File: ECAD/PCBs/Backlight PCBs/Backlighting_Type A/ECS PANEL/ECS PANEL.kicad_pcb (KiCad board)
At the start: 2 copper layers, 133.6 x 93 mm, 146 parts, among them J1 Conn_01x04_Female, J2 Conn_01x04_Female

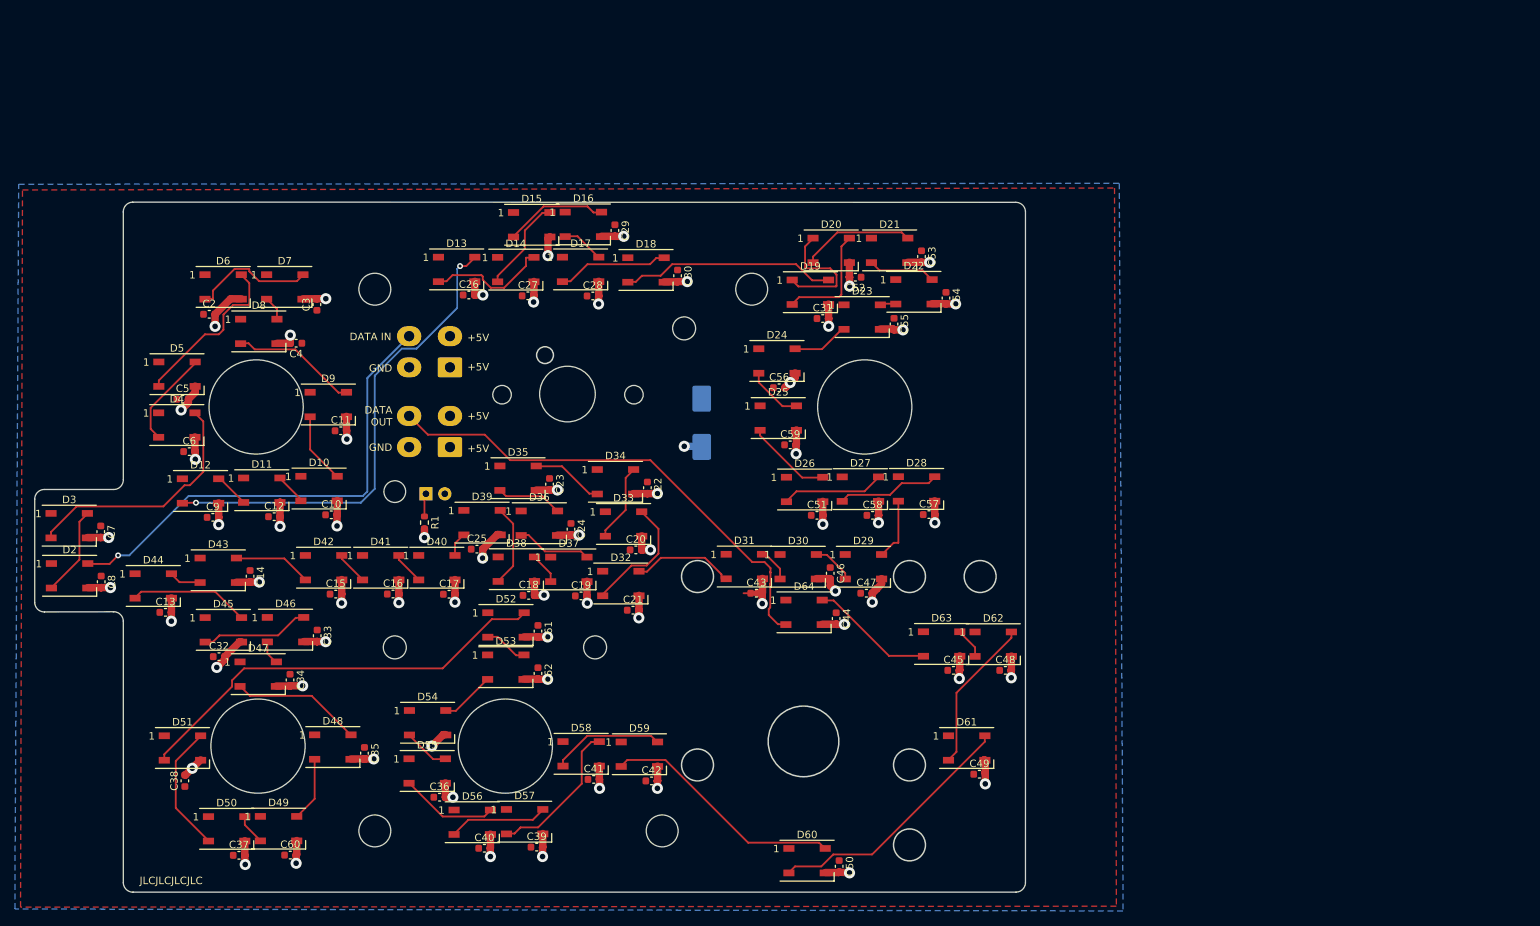
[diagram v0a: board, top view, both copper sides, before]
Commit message: Drawing Sheet & Silkscreen update - Backlight Panels(An - Fc)
1:  Updated/Relinked Drawing Sheet for both PCB and Schematics
2:  Standardized Silkscreen (if required)
3:  Added WS2812B symbol to OH Library (for future schematic fixing)

ANT SEL thru FCS PANEL
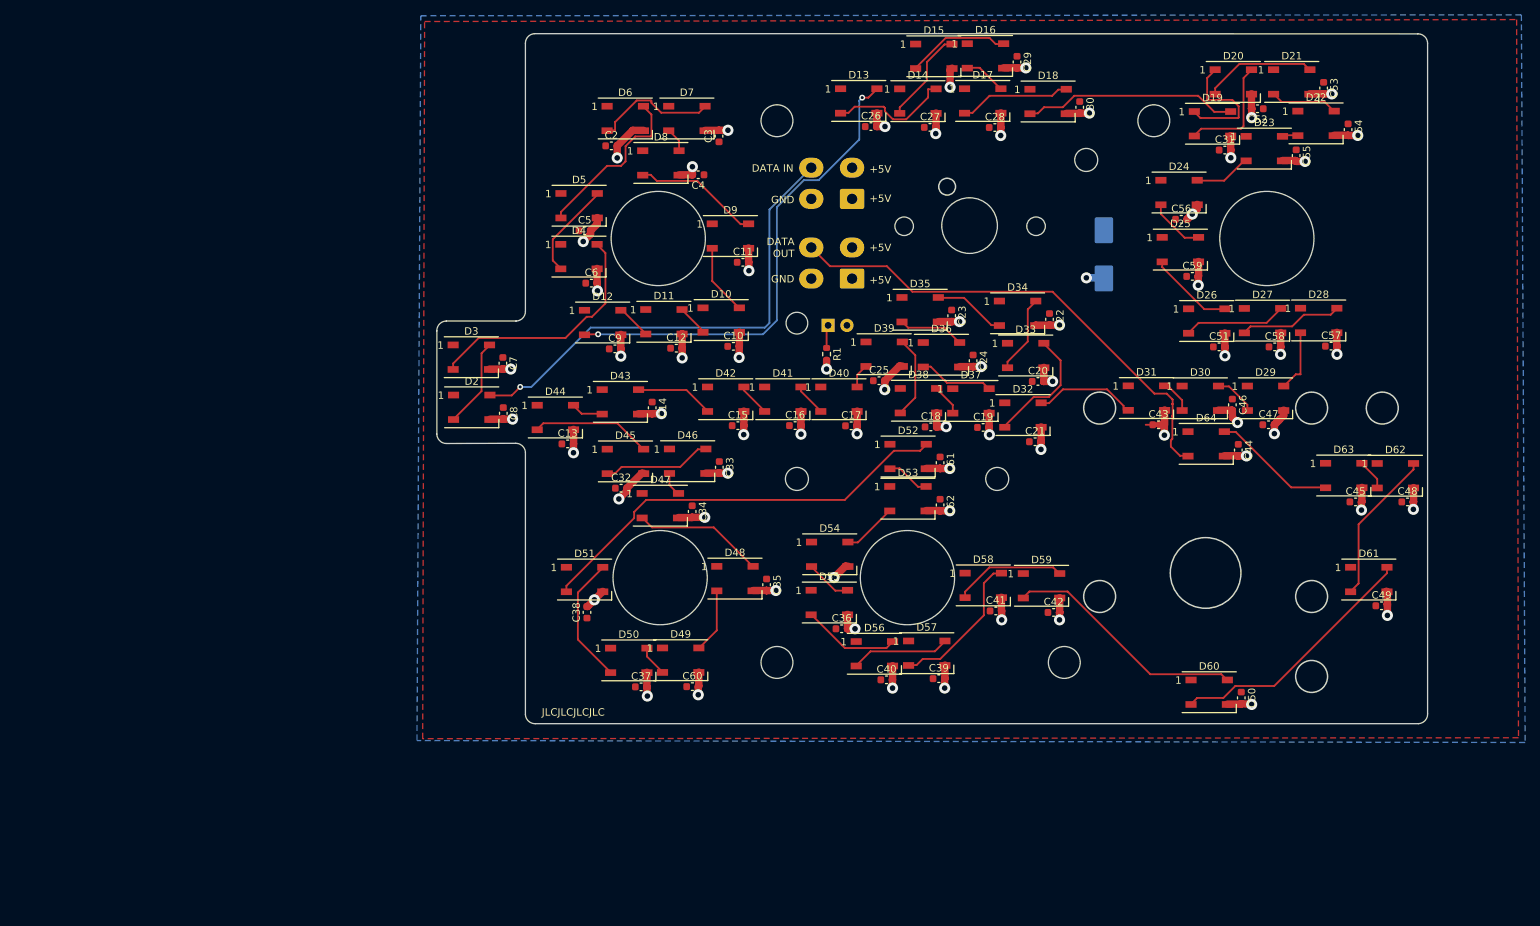
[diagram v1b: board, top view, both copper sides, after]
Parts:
- moved G*** 63.7 mm to (104.0, 93.6)
- moved C17 58.8 mm to (131.5, 97.1)
- moved C25 58.8 mm to (135.3, 91.1)
- moved C26 58.8 mm to (134.2, 56.8)
- moved C31 58.8 mm to (181.9, 60.0)
- moved C40 58.8 mm to (136.3, 131.4)
- moved C43 58.8 mm to (173.0, 97.0)
- moved C46 58.8 mm to (182.9, 94.3)
- moved C5 58.8 mm to (95.6, 70.8)
- moved C59 58.8 mm to (177.5, 77.0)
- moved D12 58.8 mm to (98.0, 83.2)
- moved D13 58.8 mm to (132.5, 53.3)
- moved D15 58.8 mm to (142.7, 47.3)
- moved D17 58.8 mm to (149.3, 53.3)
- moved D18 58.8 mm to (158.1, 53.4)
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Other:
- board text added: "ECS PANEL Revision: 3 www.openhornet.com"
- board text removed: "ECS Panel Backlight Designed by L. Walker"
- board text removed: "Version 2.0"

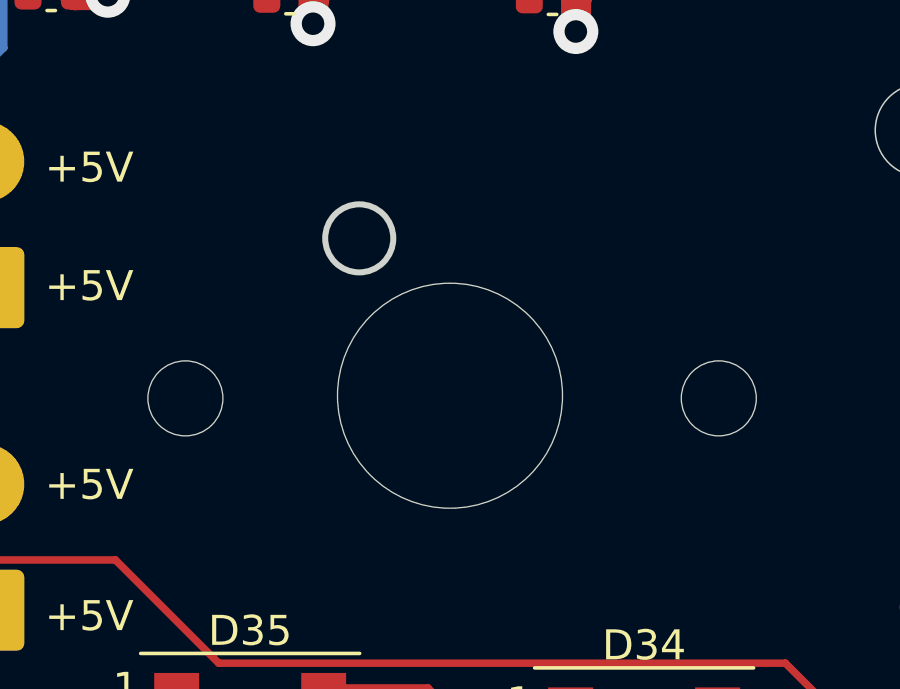
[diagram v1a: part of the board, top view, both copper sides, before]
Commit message: Review: ECS thru FCS  100%
Reviewed/adjusted silkscreens as needed
Relinked footprints
Updated Manufacturing files
Updated PNGs and STEP files as needed.
Renamed a few PNGs for standardization
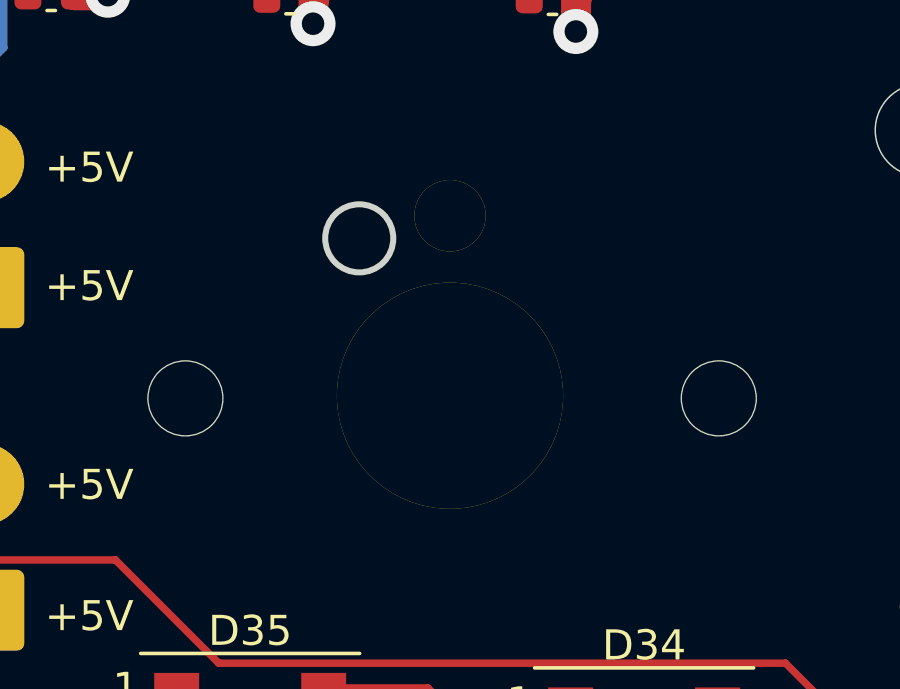
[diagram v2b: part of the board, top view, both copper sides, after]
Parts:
- 1, 3: footprint OH_Backlighting:SxAL_Toggle_13x13mm -> OH_Footprints:SxAL_Toggle_13x13mm
- 5, REF**: footprint OH_Backlighting:631H_Toggle_13mm_x_13mm -> OH_Footprints:631H_Toggle_13mm_x_13mm
- G*** (x2): footprint OH_Backlighting:S3AL_Toggle_Silkscreen -> OH_Footprints:S3AL_Toggle_Silkscreen
- G*** (x2): footprint OH_Backlighting:631H_Toggle_Silkscreen -> OH_Footprints:631H_Toggle_Silkscreen
- G***: footprint OH_General:CC-BY-NC-SA-Small -> OH_Footprints:CC-BY-NC-SA-Small
- G***: footprint OH_General:OH_LOGO_37.7mm_5.9mm -> OH_Footprints:OH_LOGO_37.7mm_5.9mm
- REF**: footprint OH_Backlighting:BR10K_Pot_11mm_x_11mm -> OH_Footprints:BR10K_Pot_11mm_x_11mm
- REF** (x4): footprint OH_Backlighting:OH_Panel_6-32_PHS -> OH_Footprints:OH_Panel_6-32_PHS
- REF** (x2): value MountingHole_2.5mm -> MountingHole; footprint MountingHole:MountingHole_2.5mm -> OH_Footprints:MountingHole_2.5mm

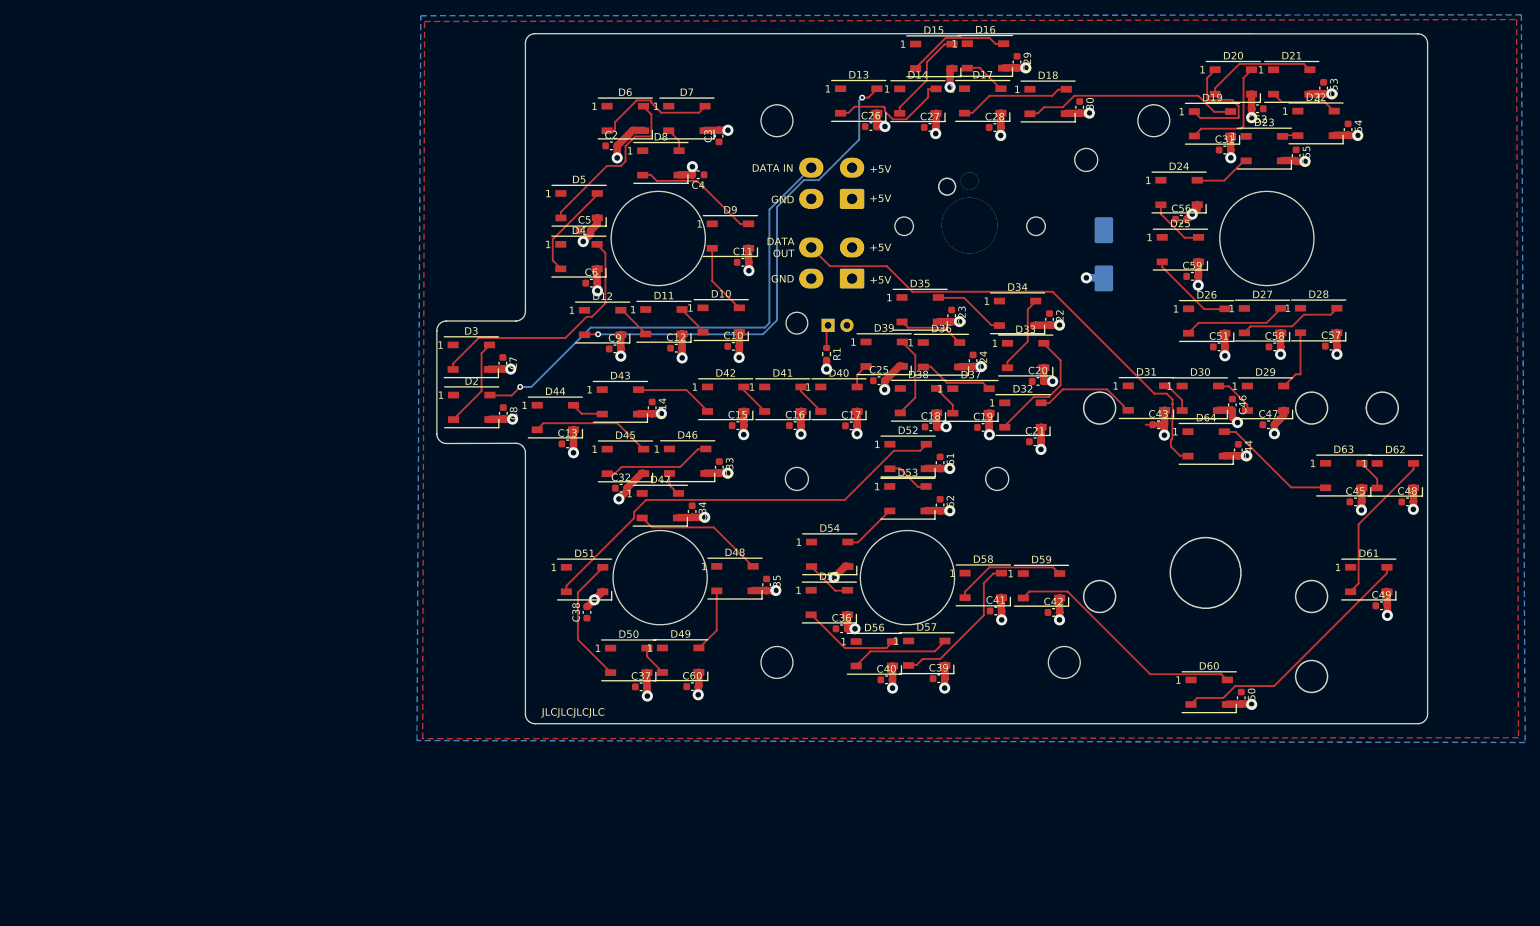
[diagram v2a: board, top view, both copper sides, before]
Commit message: KiCad 7 Transition - ECS Panel
Changed orientation of Test Point symbol in library from +90 to 0

Schematic/PCB standardization
-Consolidated BOM.  Removed excess BOMs
-Updated manufacturing files
-Fixed PCB routing after rotating a LED 90 degress.  Pad didn't have access to GND net.
-Fixed clearance issues around NPTHs
-Updated Assets (PNGs, STEP)
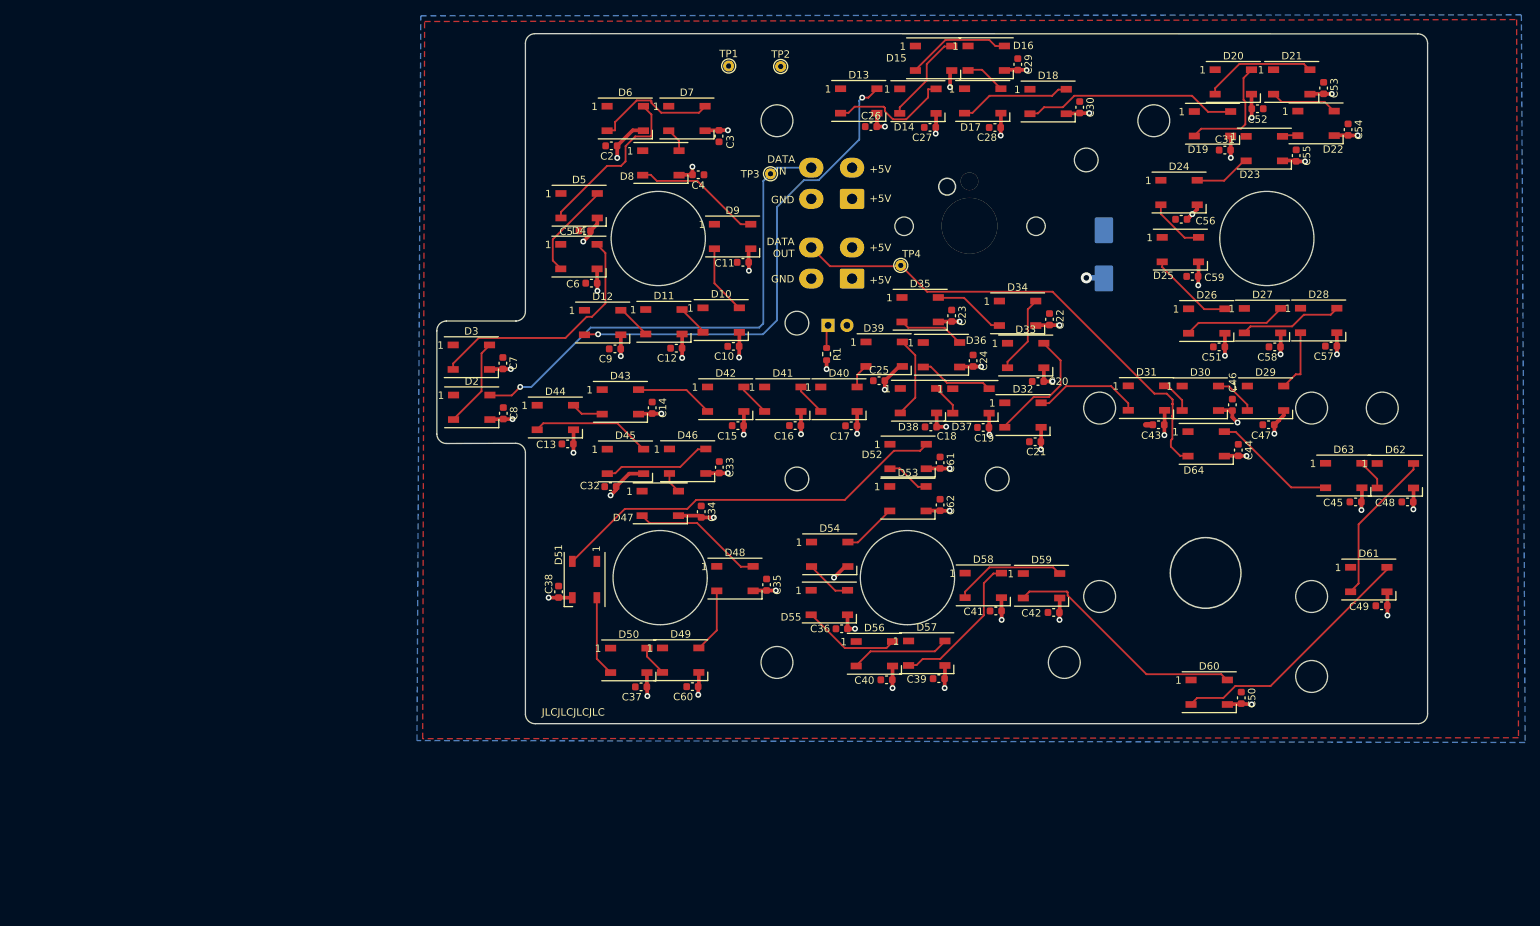
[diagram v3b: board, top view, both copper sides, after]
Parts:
- removed 1, 3: SxAL_Toggle_13x13mm, OH_Footprints:SxAL_Toggle_13x13mm
- removed 5, REF**: 631H_Toggle_13mm_x_13mm, OH_Footprints:631H_Toggle_13mm_x_13mm
- removed REF**: BR10K_Pot_11mm_x_11mm, OH_Footprints:BR10K_Pot_11mm_x_11mm
- removed REF** (x4): OH_Panel_Fastner_Keepout, OH_Footprints:OH_Panel_6-32_PHS
- removed REF** (x2): MountingHole, OH_Footprints:MountingHole_2.5mm
- added MH1: 6x32 / 4mm, OH_Footprints:MountingHole_6-32_PHS, B.Cu at (121.5, 56.0)
- added MH10: 6x32 / 4mm, OH_Footprints:MountingHole_6-32_PHS, B.Cu at (193.6, 130.9)
- added MH11: M3 / 3.2mm, OH_Footprints:MountingHole_3.2mm_M3_DIN965, B.Cu at (163.2, 61.3)
- added MH12: M3 / 3.2mm, OH_Footprints:MountingHole_3.2mm_M3_DIN965, B.Cu at (124.2, 83.3)
- added MH13: M3 / 3.2mm, OH_Footprints:MountingHole_3.2mm_M3_DIN965, B.Cu at (124.2, 104.3)
- added MH14: M3 / 3.2mm, OH_Footprints:MountingHole_3.2mm_M3_DIN965, B.Cu at (151.2, 104.3)
- added MH15: 2.5mm, OH_Footprints:MountingHole_2.5mm, B.Cu at (138.7, 70.2)
- added MH16: 2.5mm, OH_Footprints:MountingHole_2.5mm, B.Cu at (156.4, 70.2)
- added MH17: Switch_NKK SxAL, OH_Footprints:SxAL_Toggle_13x13mm, F.Cu at (105.5, 71.9)
- added MH18: Switch_NKK SxAL, OH_Footprints:SxAL_Toggle_13x13mm, F.Cu at (187.6, 71.9)
- added MH19: Switch_631H, OH_Footprints:631HX_Toggle_13mm_x_13mm, F.Cu at (105.8, 117.6)
- added MH2: 6x32 / 4mm, OH_Footprints:MountingHole_6-32_PHS, B.Cu at (172.3, 56.0)
- added MH20: Switch_631H, OH_Footprints:631HX_Toggle_13mm_x_13mm, F.Cu at (139.1, 117.6)
- added MH21: Pot_B10K, OH_Footprints:BR10K_Pot_11mm_x_11mm, F.Cu at (147.5, 70.2)
- added MH3: 6x32 / 4mm, OH_Footprints:MountingHole_6-32_PHS, B.Cu at (165.0, 94.7)
- added MH4: 6x32 / 4mm, OH_Footprints:MountingHole_6-32_PHS, B.Cu at (193.6, 94.7)
- added MH5: 6x32 / 4mm, OH_Footprints:MountingHole_6-32_PHS, B.Cu at (203.1, 94.7)
- added MH6: 6x32 / 4mm, OH_Footprints:MountingHole_6-32_PHS, B.Cu at (165.0, 120.1)
- added MH7: 6x32 / 4mm, OH_Footprints:MountingHole_6-32_PHS, B.Cu at (193.6, 120.1)
- added MH8: 6x32 / 4mm, OH_Footprints:MountingHole_6-32_PHS, B.Cu at (121.5, 129.0)
- added MH9: 6x32 / 4mm, OH_Footprints:MountingHole_6-32_PHS, B.Cu at (160.3, 129.0)
- added TP1: TestPoint, OH_Footprints:TestPoint_THTPad_D1.5mm_Drill0.7mm, F.Cu at (115.0, 48.6)
- added TP2: TestPoint, OH_Footprints:TestPoint_THTPad_D1.5mm_Drill0.7mm, F.Cu at (122.0, 48.7)
- added TP3: TestPoint, OH_Footprints:TestPoint_THTPad_D1.5mm_Drill0.7mm, F.Cu at (120.6, 63.2)
- added TP4: TestPoint, OH_Footprints:TestPoint_THTPad_D1.5mm_Drill0.7mm, F.Cu at (138.2, 75.5)
- C1: value C_Polarized -> 1000uF
- C10, C11, C12, C13, C14, C15, C16, C17, C18, C19, C2, C20, C21, C22, C23, C24, C25, C26, C27, C28, C29, C3, C30, C31, C32, C33, C34, C35, C36, C37, C38, C39, C4, C40, C41, C42, C43, C44, C45, C46, C47, C48, C49, C5, C50, C51, C52, C53, C54, C55, C56, C57, C58, C59, C6, C60, C61, C62, C7, C8, C9: value C -> 0.1uF
- D1: value LED -> Green
- G*** (x2): moved to B.Cu
- G***: footprint OH_Footprints:631H_Toggle_Silkscreen -> OH_Footprints:631H2_Toggle_Silkscreen; moved to B.Cu
- G***: footprint OH_Footprints:631H_Toggle_Silkscreen -> OH_Footprints:631H3_Toggle_Silkscreen; moved to B.Cu
- J1, J2: value Conn_01x04_Female -> Mini-Fit Jr. 2x02
- LOGO1: renamed from G***; footprint OH_Footprints:OH_LOGO_37.7mm_5.9mm -> OH_Footprints:LOGO_OH_Text_Large
- LOGO2: renamed from G***; footprint OH_Footprints:CC-BY-NC-SA-Small -> OH_Footprints:LOGO_CC-BY-NC-SA_Half_Small
- R1: value R -> 470
- moved LOGO1 8.96 mm to (147.6, 97.4)
- moved C38 4.73 mm to (92.1, 119.5), turned to -90 degrees
- moved C32 1.46 mm to (99.1, 105.3)
- moved G*** 1.42 mm to (96.3, 71.9), turned to 180 degrees
- moved G*** 1.29 mm to (178.7, 72.3), turned to 180 degrees
- moved C34 1.22 mm to (111.3, 108.7)
- moved G*** 1.03 mm to (128.4, 117.6), turned to 180 degrees
- moved G*** 1.02 mm to (95.1, 117.4), turned to 180 degrees
- moved D16 0.33 mm to (149.7, 47.6)
- moved C29 0.33 mm to (154.0, 48.4)
- moved D47 0.31 mm to (105.8, 107.6)
- moved D9 0.30 mm to (115.5, 71.6)
- moved D15 0.27 mm to (142.6, 47.6)
- turned D51 to -90 degrees
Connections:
- net /DATAIN renamed DATA IN
- net /DATAOUT renamed DATA OUT
- net /LED+5V renamed +5V
- net /LEDGND renamed GND
- net Net-(D14-Pad2) renamed /DATA1
- net Net-(D27-Pad2) renamed /DATA2
- net Net-(D40-Pad2) renamed /DATA3
- net Net-(D53-Pad2) renamed /DATA4
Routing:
- net +5V: track 20.2 -> 3.22 mm
- net Net-(D50-DOUT): track 17.3 -> 10.9 mm
- net Net-(D51-DOUT): track 57.6 -> 54.2 mm
- net DATA IN: track 65.0 -> 67.3 mm
- net DATA OUT: track 68.3 -> 66.6 mm
- net GND: track 205.3 -> 203.6 mm
- net Net-(D31-DOUT): track 13.4 -> 14.6 mm
- net Net-(D30-DOUT): track 5.12 -> 4.01 mm
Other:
- outline, holes or cut-outs redrawn
- board text added: "0.2000 mm"
- board text added: "0.2000 mm / 0.1270 mm"
- board text added: "1.6000 mm"
- board text added: "133.5532 mm x 93.0148 mm"
- board text added: "BOARD CHARACTERISTICS"
- board text added: "Board Thickness:"
- board text added: "Board overall dimensions:"
- board text added: "Castellated pads:"
- board text added: "Copper Finish:"
- board text added: "Copper Layer Count:"
- board text added: "ECS PANEL REV: 4 WWW.OPENHORNET.COM"
- board text added: "Edge card connectors:"
- board text added: "Impedance Control:"
- board text added: "Min hole diameter:"
- board text added: "Min track/spacing:"
- board text added: "No"
- board text added: "None"
- board text added: "Plated Board Edge:"
- board text removed: "3"
- board text removed: "BLEED AIR"
- board text removed: "ECS PANEL Revision: 3 www.openhornet.com"
- board text removed: "IN"
- board text removed: "Switch PCB H1"
- board text removed: "Switch PCB H2"
- board text removed: "Switch PCB H3"
- board text removed: "Switch PCB H4"
- board text removed: "THRU"
- board text removed: "⌀3MM"
- board text removed: "⌀4MM"
